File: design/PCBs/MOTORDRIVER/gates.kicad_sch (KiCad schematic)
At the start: 9 parts, among them Q1 SI4532CDY-T1-GE3, Q2 SI4532CDY-T1-GE3, Q27 SI4532CDY-T1-GE3, Q3 SI4532CDY-T1-GE3, Q30 SI4532CDY-T1-GE3, Q33 SI4532CDY-T1-GE3, Q34 SI4532CDY-T1-GE3, Q35 SI4532CDY-T1-GE3, Q4 SI4532CDY-T1-GE3

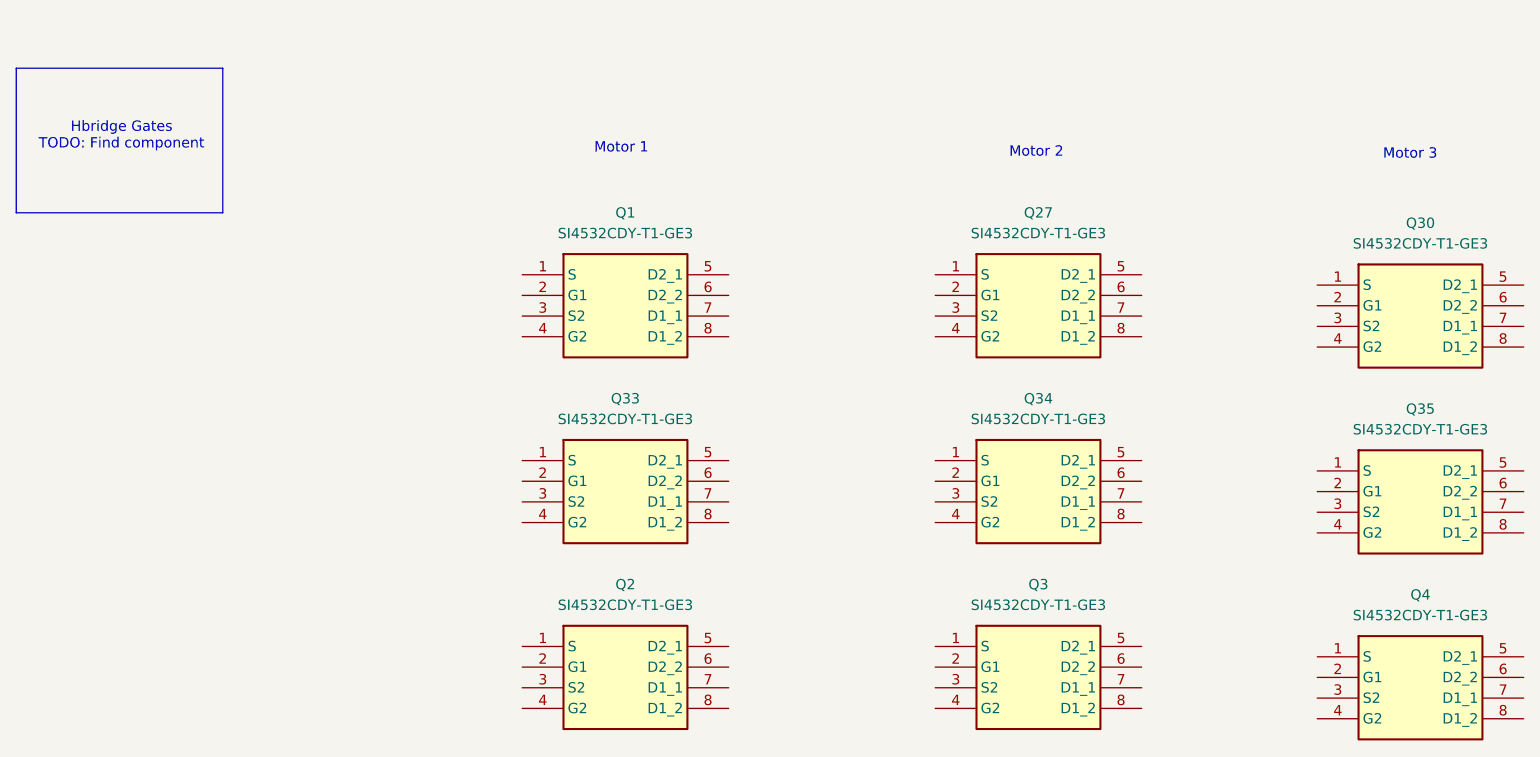
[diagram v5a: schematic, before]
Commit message: Motor headers added, mosfet datasheets
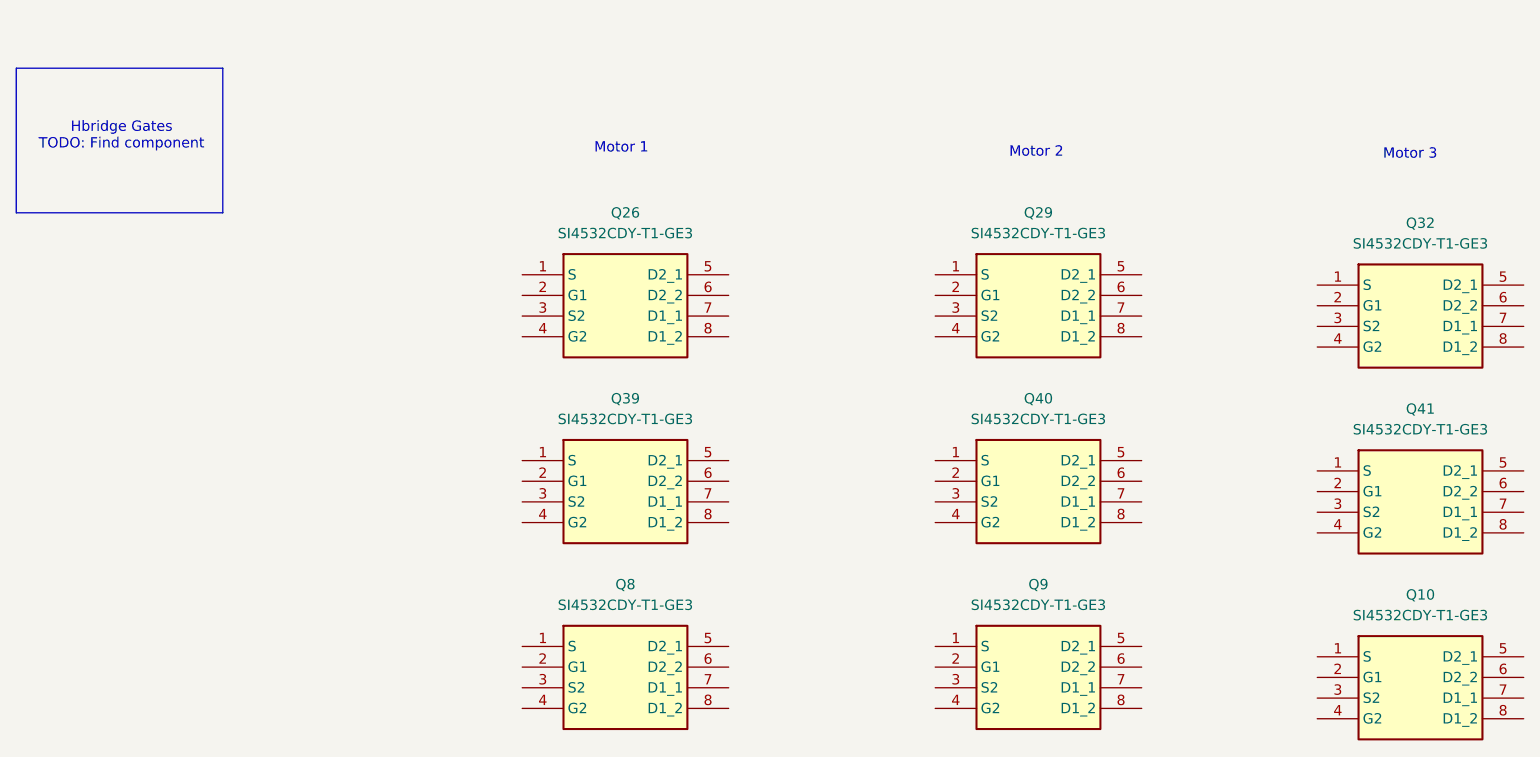
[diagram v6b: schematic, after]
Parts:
- renumbered Q4 to Q10, Q1 to Q26, Q27 to Q29, Q30 to Q32, Q33 to Q39, Q34 to Q40, Q35 to Q41, Q2 to Q8, Q3 to Q9
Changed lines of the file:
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@@
 		(dnp no)
 		(fields_autoplaced yes)
-		(property "Reference" "Q33"
+		(property "Reference" "Q39"
 			(at 130.81 93.98 0)
 			(effects
@@
 		(dnp no)
 		(fields_autoplaced yes)
-		(property "Reference" "Q30"
+		(property "Reference" "Q32"
 			(at 228.6 72.39 0)
 			(effects
@@
 		(dnp no)
 		(fields_autoplaced yes)
-		(property "Reference" "Q1"
+		(property "Reference" "Q26"
 			(at 130.81 71.12 0)
 			(effects
@@
 		(dnp no)
 		(fields_autoplaced yes)
-		(property "Reference" "Q2"
+		(property "Reference" "Q8"
 			(at 130.81 116.84 0)
 			(effects
@@
 		(dnp no)
 		(fields_autoplaced yes)
-		(property "Reference" "Q34"
+		(property "Reference" "Q40"
 			(at 181.61 93.98 0)
 			(effects
@@
 		(dnp no)
 		(fields_autoplaced yes)
-		(property "Reference" "Q35"
+		(property "Reference" "Q41"
 			(at 228.6 95.25 0)
 			(effects
@@
 		(dnp no)
 		(fields_autoplaced yes)
-		(property "Reference" "Q3"
+		(property "Reference" "Q9"
 			(at 181.61 116.84 0)
 			(effects
@@
 		(dnp no)
 		(fields_autoplaced yes)
-		(property "Reference" "Q27"
+		(property "Reference" "Q29"
 			(at 181.61 71.12 0)
 			(effects
@@
 		(dnp no)
 		(fields_autoplaced yes)
-		(property "Reference" "Q4"
+		(property "Reference" "Q10"
 			(at 228.6 118.11 0)
 			(effects

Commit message: Mosfet symbol added
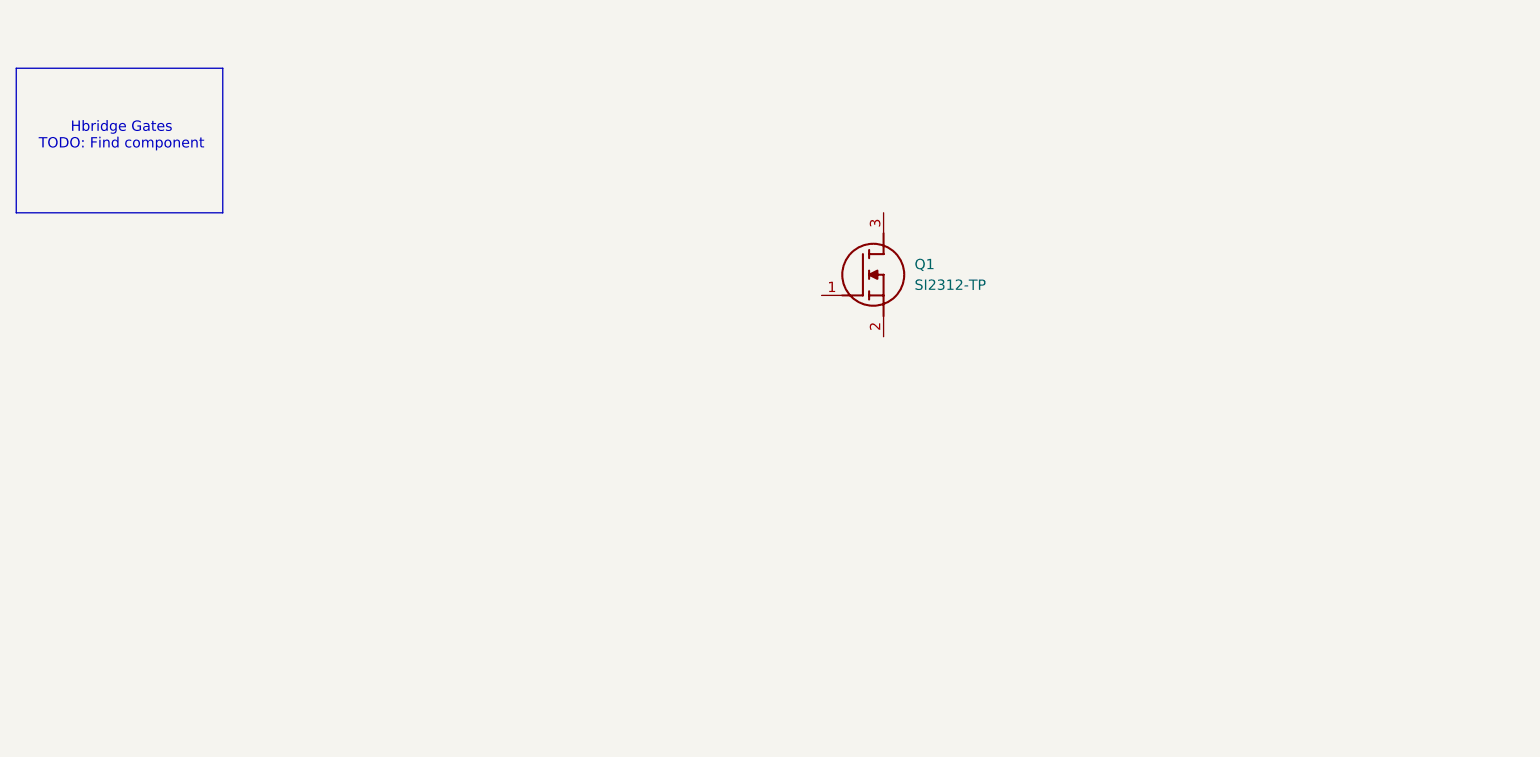
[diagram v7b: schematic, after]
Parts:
- removed Q10, Q26, Q29, Q32, Q39, Q40, Q41, Q8, Q9: SI4532CDY-T1-GE3, SOT127P600X175-8N, symbol SI4532CDY-T1-GE3:SI4532CDY-T1-GE3
- added Q1: SI2312-TP, SOT95P237X125-3N, symbol SI2312-TP:SI2312-TP
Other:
- note removed: "Motor 1"
- note removed: "Motor 2"
- note removed: "Motor 3"

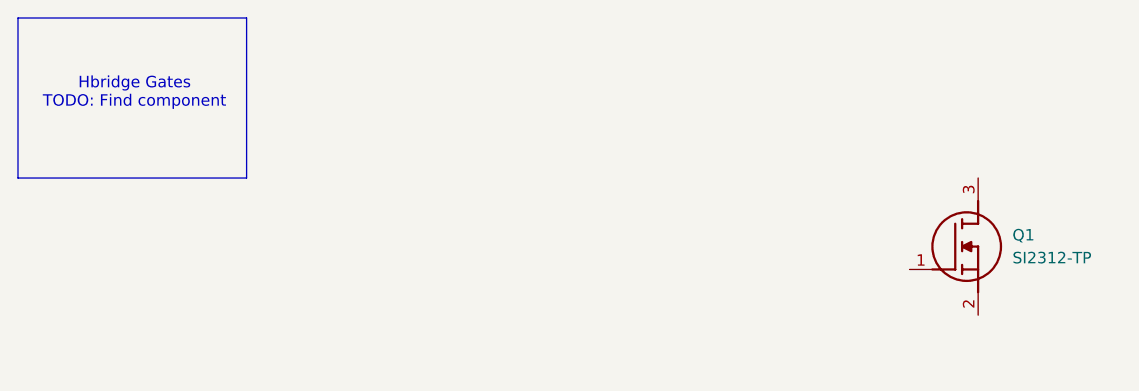
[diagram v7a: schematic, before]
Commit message: added gate driver
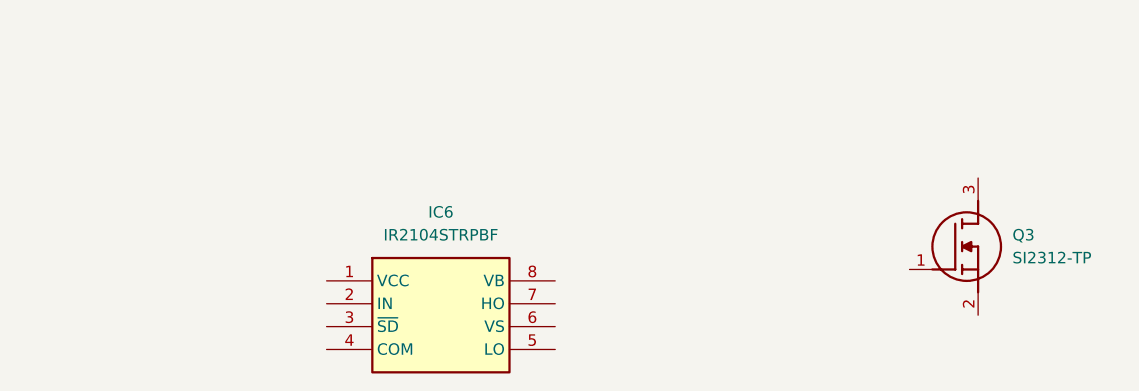
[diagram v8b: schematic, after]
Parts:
- added IC6: IR2104STRPBF, SOIC127P600X175-8N, symbol IR2104STRPBF:IR2104STRPBF
- renumbered Q1 to Q3
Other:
- note removed: "Hbridge Gates TODO: Find component"
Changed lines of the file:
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@@
 	(generator_version "8.0")
 	(paper "A4")
-	(rectangle
-		(start 55.88 53.34)
-		(end 81.28 71.12)
-		(stroke
-			(width 0)
-			(type default)
+	(symbol
+		(lib_id "IR2104STRPBF:IR2104STRPBF")
+		(at 90.17 82.55 0)
+		(unit 1)
+		(exclude_from_sim no)
+		(in_bom yes)
+		(on_board yes)
+		(dnp no)
+		(fields_autoplaced yes)
+		(property "Reference" "IC6"
+			(at 102.87 74.93 0)
+			(effects
+				(font
+					(size 1.27 1.27)
+				)
+			)
 		)
-		(fill
-			(type none)
+		(property "Value" "IR2104STRPBF"
+			(at 102.87 77.47 0)
+			(effects
+				(font
+					(size 1.27 1.27)
+				)
+			)
 		)
-	)
-	(text "Hbridge Gates\nTODO: Find component"
-		(exclude_from_sim no)
-		(at 68.834 61.722 0)
-		(effects
-			(font
-				(size 1.27 1.27)
+		(property "Footprint" "SOIC127P600X175-8N"
+			(at 111.76 177.47 0)
+			(effects
+				(font
+					(size 1.27 1.27)
+				)
+				(justify left top)
+				(hide yes)
+			)
+		)
+		(property "Datasheet" "https://www.infineon.com/cms/en/product/power/gate-driver-ics/?"
+			(at 111.76 277.47 0)
+			(effects
+				(font
+					(size 1.27 1.27)
+				)
+				(justify left top)
+				(hide yes)
+			)
+		)
+		(property "Description" "MOSFET Driver, Dual, 8 Pin, Plastic, SOP"
+			(at 90.17 82.55 0)
+			(effects
+				(font
+					(size 1.27 1.27)
+				)
+				(hide yes)
+			)
+		)
+		(property "Height" "1.75"
+			(at 111.76 477.47 0)
+			(effects
+				(font
+					(size 1.27 1.27)
+				)
+				(justify left top)
+				(hide yes)
+			)
+		)
+		(property "Mouser Part Number" "942-IR2104STRPBF"
+			(at 111.76 577.47 0)
+			(effects
+				(font
+					(size 1.27 1.27)
+				)
+				(justify left top)
+				(hide yes)
+			)
+		)
+		(property "Mouser Price/Stock" "https://www.mouser.co.uk/ProductDetail/Infineon-Technologies/IR2104STRPBF?qs=2r01AXMCG3NCbspWVHqTYw%3D%3D"
+			(at 111.76 677.47 0)
+			(effects
+				(font
+					(size 1.27 1.27)
+				)
+				(justify left top)
+				(hide yes)
+			)
+		)
+		(property "Manufacturer_Name" "Infineon"
+			(at 111.76 777.47 0)
+			(effects
+				(font
+					(size 1.27 1.27)
+				)
+				(justify left top)
+				(hide yes)
+			)
+		)
+		(property "Manufacturer_Part_Number" "IR2104STRPBF"
+			(at 111.76 877.47 0)
+			(effects
+				(font
+					(size 1.27 1.27)
+				)
+				(justify left top)
+				(hide yes)
+			)
+		)
+		(pin "1"
+		)
+		(pin "2"
+		)
+		(pin "7"
+		)
+		(pin "8"
+		)
+		(pin "5"
+		)
+		(pin "6"
+		)
+		(pin "3"
+		)
+		(pin "4"
+		)
+		(instances
+			(project ""
+				(path "/c7634e88-16d1-45ec-9aac-9c841e03cf6d/4adc8e75-6797-461c-8ad6-e6b779b2e551"
+					(reference "IC8")
+					(unit 1)
+				)
+				(path "/c7634e88-16d1-45ec-9aac-9c841e03cf6d/b5eb0271-9027-4941-b236-8f001fce8a08"
+					(reference "IC6")
+					(unit 1)
+				)
+				(path "/c7634e88-16d1-45ec-9aac-9c841e03cf6d/d2c99155-6dc4-4cef-b7d8-f7ba5e4118d0"
+					(reference "IC7")
+					(unit 1)
+				)
 			)
 		)
@@
 		(dnp no)
 		(fields_autoplaced yes)
-		(property "Reference" "Q1"
+		(property "Reference" "Q3"
 			(at 166.37 77.4699 0)
 			(effects
